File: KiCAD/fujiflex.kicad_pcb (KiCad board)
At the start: 2 copper layers, 27.7 x 30 mm, 35 parts, among them J1 505278-1933, U1 XC3S200A-4VQG100C, U2 AT25SF041B-MAHD-T, U3 AP2127N-1.2

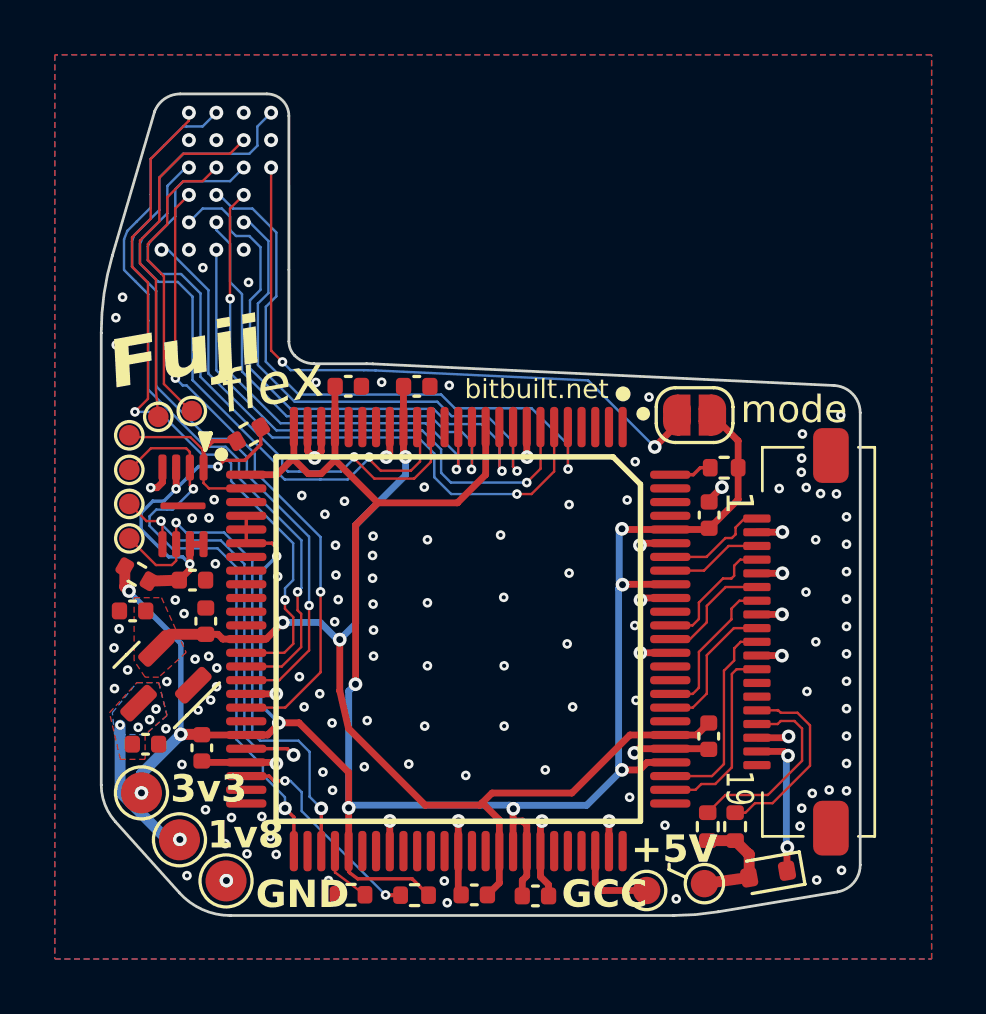
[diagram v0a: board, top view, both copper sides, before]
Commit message: minor routing fixes
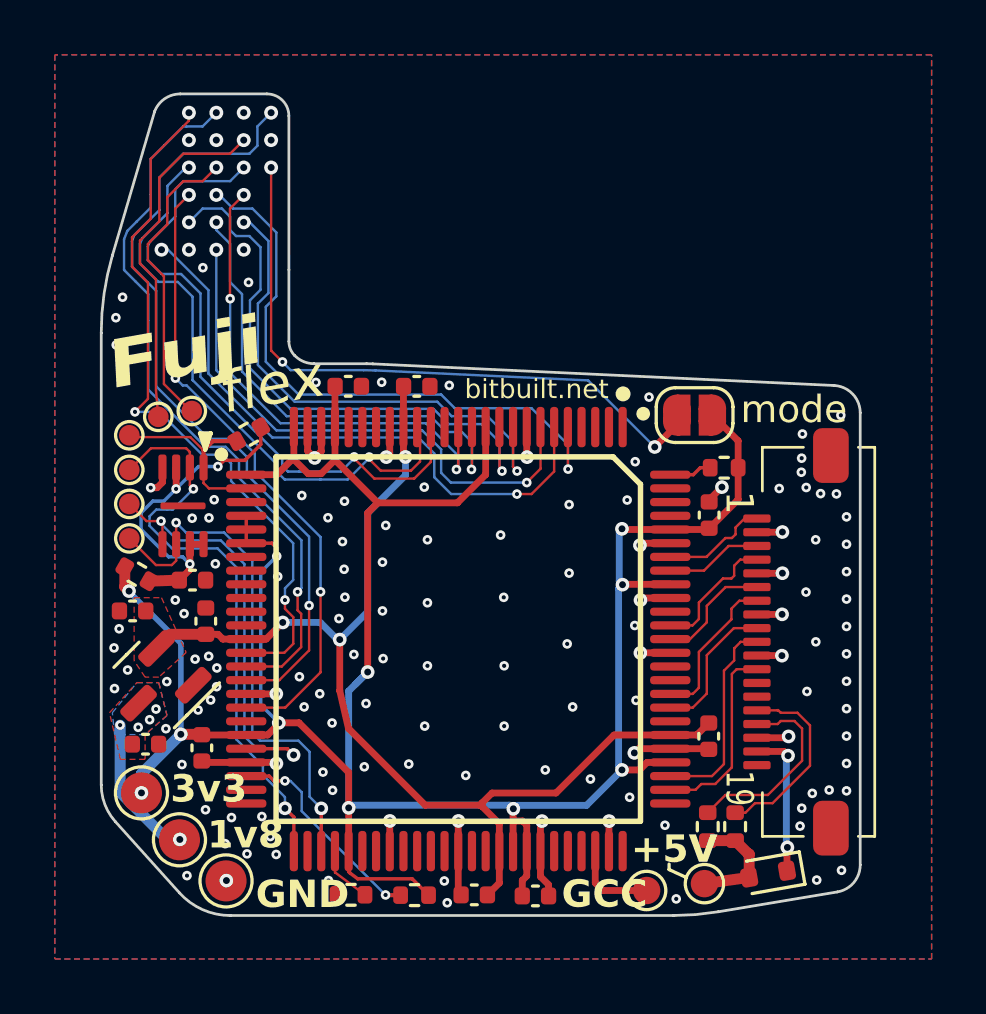
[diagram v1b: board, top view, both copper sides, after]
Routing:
- net +3.3V: track 96.6 -> 97.2 mm

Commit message: fix LDO blunder
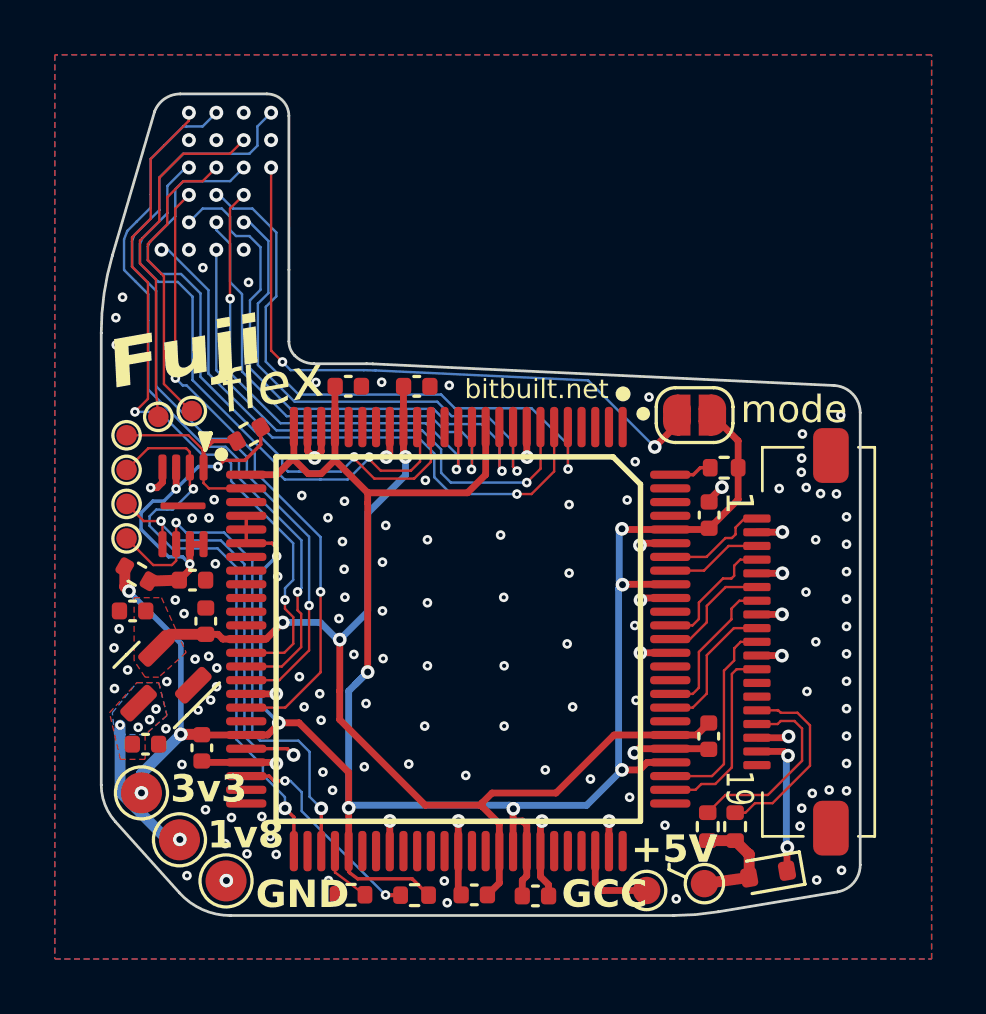
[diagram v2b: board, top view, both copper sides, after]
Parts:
- U3: value AP2127N-1.2 -> TPS7A0512PDBZR
- moved TP6 0.10 mm to (131.9, 94.3)
- moved TP7 0.10 mm to (131.9, 96.8)
- moved TP8 0.10 mm to (131.9, 95.6)
- moved TP9 0.10 mm to (131.9, 98.1)

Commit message: pcb fixes
- tie IR button pin high
- minor layout/routing tweaks
- silkscreen edits
- updated gerbers
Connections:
- U1 pad 70: unconnected-(U1-IO_L05P_1-Pad70) -> +3.3V
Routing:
- net +3.3V: track 97.1 -> 99.1 mm, vias 11 -> 12

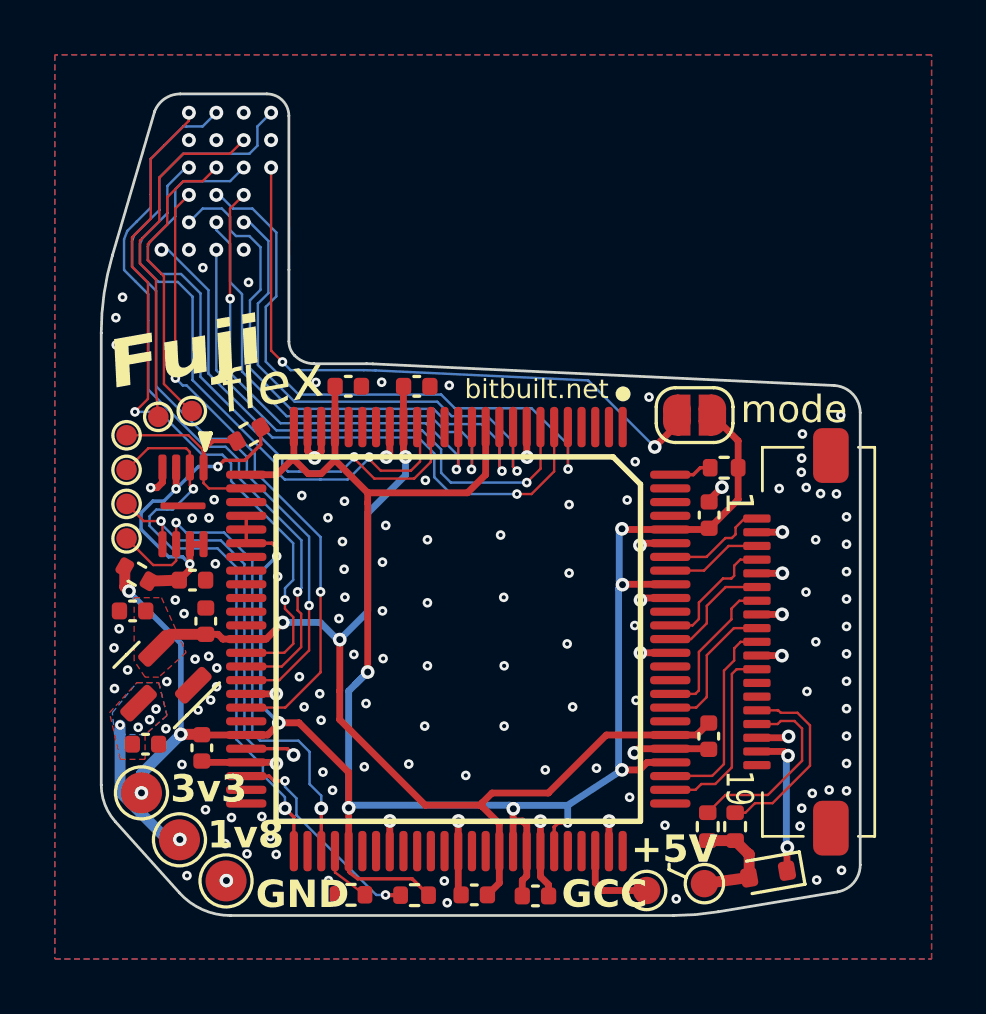
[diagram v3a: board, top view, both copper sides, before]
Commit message: minor layout updates
-updated grounding and some via sizes
-fixed IR button on 6L version
-updated gerbers
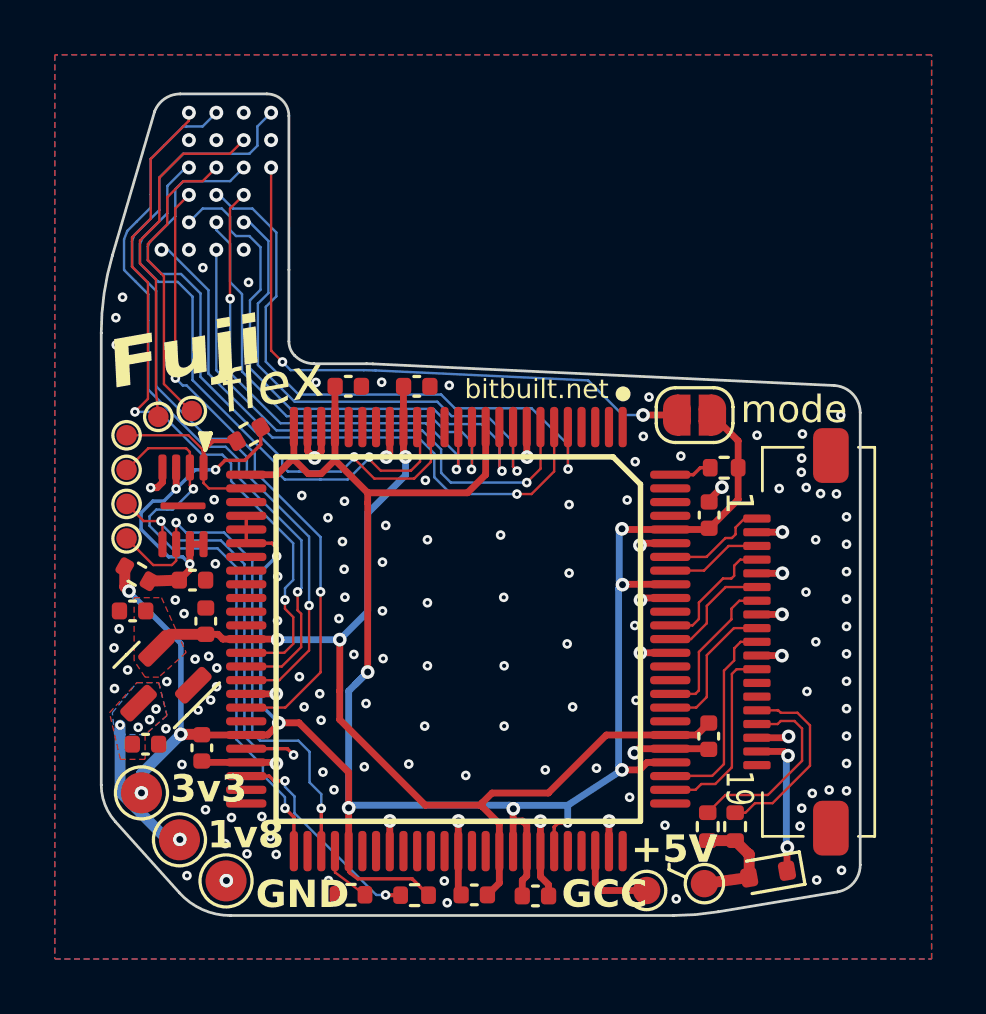
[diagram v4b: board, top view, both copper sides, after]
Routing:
- net MODE: track 23.5 -> 22.3 mm
- net +1V2: track 40.5 -> 40.0 mm
- net GND: vias 135 -> 139
